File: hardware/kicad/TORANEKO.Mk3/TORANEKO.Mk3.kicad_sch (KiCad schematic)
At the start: 85 parts, among them IC1 MP6551GQB-P, IC2 MP6551GQB-P, IC3 NCR321PASX, IC4 NCR321PASX, IC5 AS5047P-ATSM, IC6 STM32F411CEU6TR, IC7 AS5047P-ATSM, IC8 NCR321PASX, IC9 NCR321PASX, J1 Conn_01x02_Pin, J2 Conn_01x02_Pin, J3 Conn_01x02_Male, J5 Conn_01x02_Pin, J6 Conn_02x03_Odd_Even, Q1 IRLML6402, Q5 IRLML6344, SW1 SW_Push, U1 LSM6DSRXTR, U2 LXDC55FAAA-203, U3 Encord, U4 Encord_B, U5 Encord, U6 Encord_B, Y1 CSTNE10M0G52Z000R0

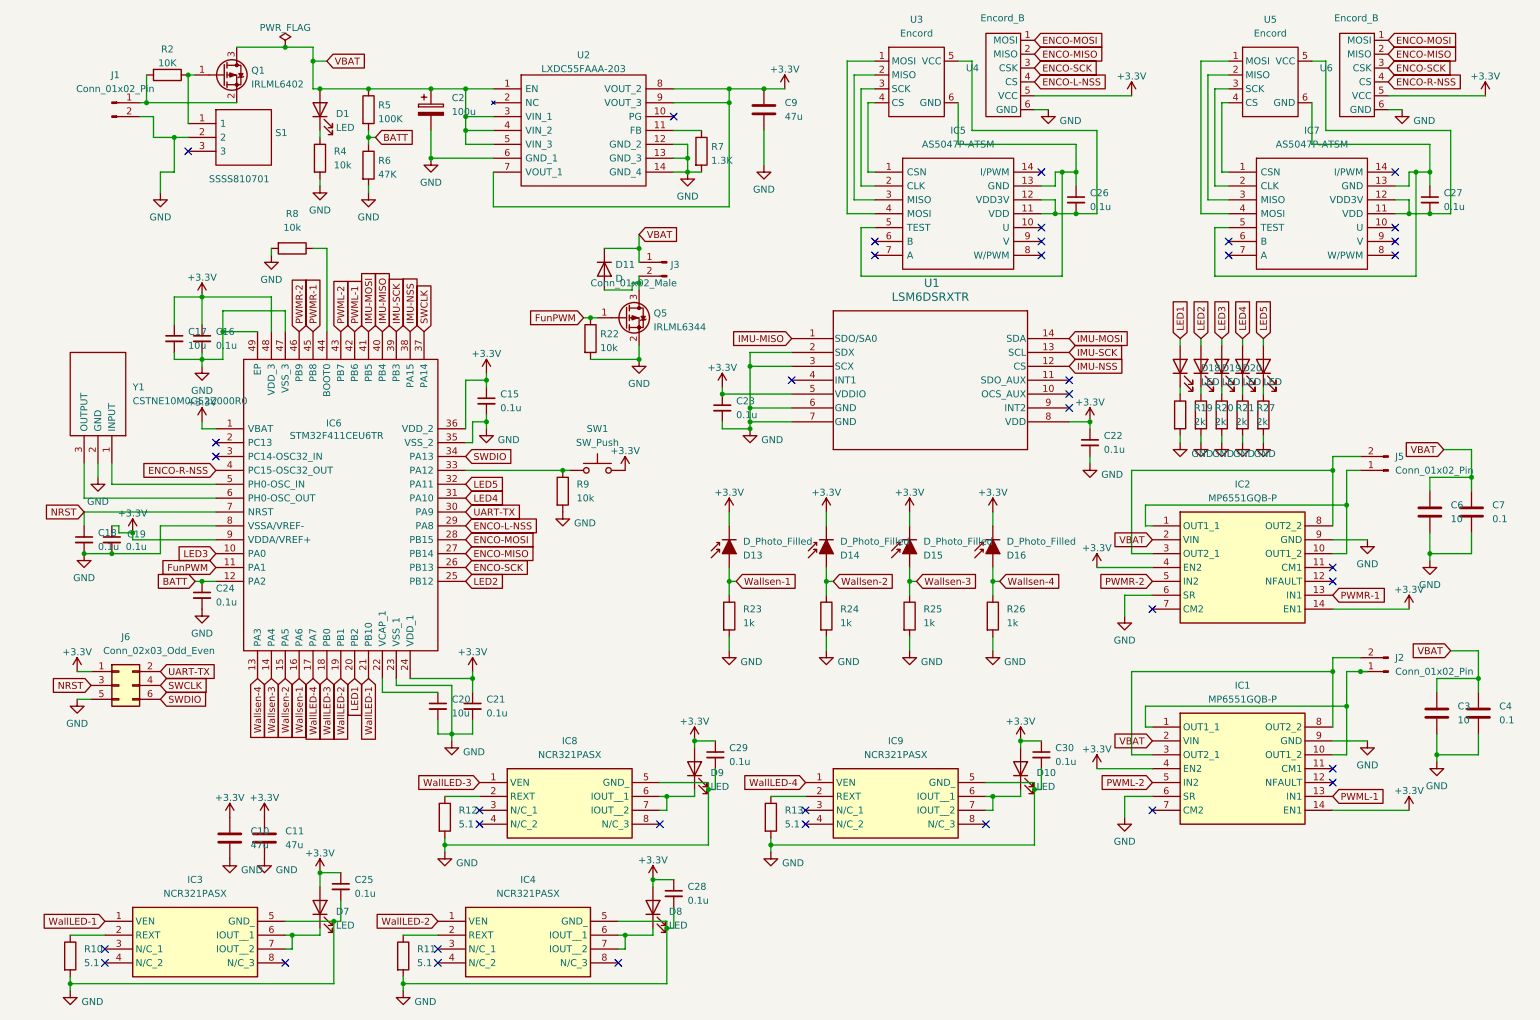
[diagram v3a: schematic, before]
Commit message: Start TORANEKO.Mk3 PCB layout; update schematic; add motor mount DXF
- Import schematic into PCB and start board layout (.kicad_pcb)
- Schematic: re-add LED/resistor pairs D23/R29, D24/R30 (2k) and connector J4;
  rework LED / WallLED global labels
- Add motor mount outline DXF

Co-Authored-By: Claude Opus 5.5 <noreply@anthropic.com>
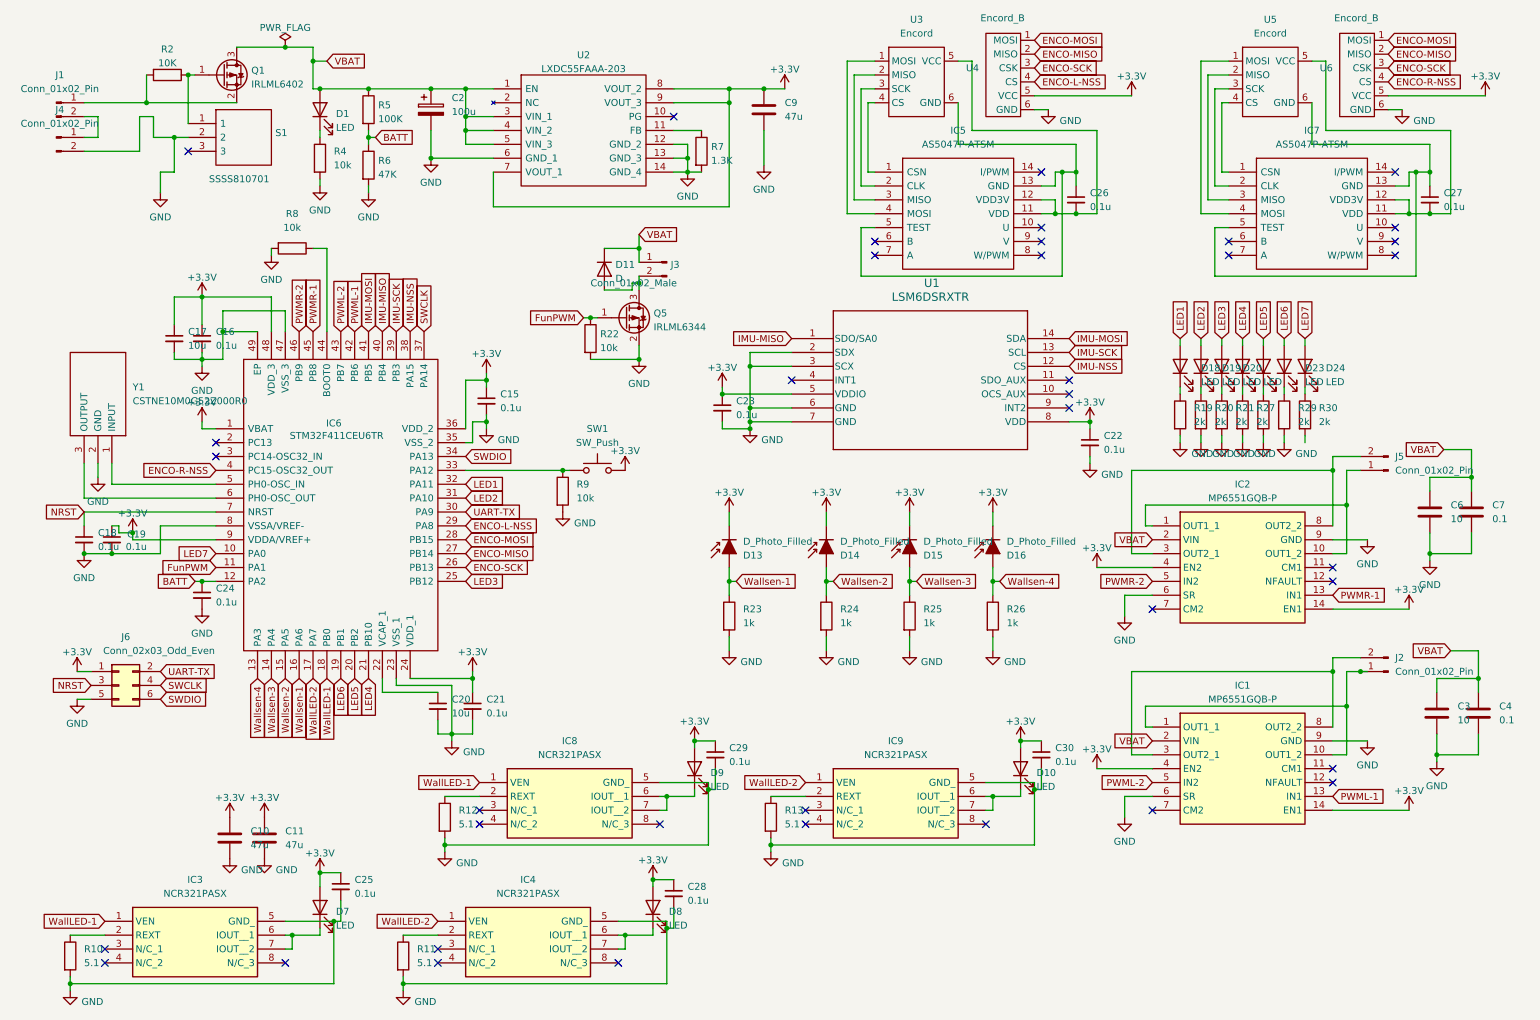
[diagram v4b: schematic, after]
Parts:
- added D23, D24: LED, LED_SMD:LED_0402_1005Metric, symbol Device:LED
- added J4: Conn_01x02_Pin, Connector_JST:JST_ZH_B2B-ZR_1x02_P1.50mm_Vertical, symbol Connector:Conn_01x02_Pin
- added R29, R30: 2k, Resistor_SMD:R_0402_1005Metric, symbol Device:R
- J1: footprint Connector_PinHeader_2.54mm:PinHeader_1x02_P2.54mm_Vertical -> Connector_JST:JST_ZH_B2B-ZR_1x02_P1.50mm_Vertical
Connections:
- net WallLED-3 is gone; now on net WallLED-1: IC6.18 (PB0), IC8.1 (VEN)
- net WallLED-4 is gone; now on net WallLED-2: IC6.17 (PA7), IC9.1 (VEN)
- net GND: now also J4.2 (Pin_2), R29.2; no longer J1.2 (Pin_2)
- net LED1: now also IC6.32 (PA11); no longer IC6.20 (PB2)
- net LED2: now also IC6.31 (PA10); no longer IC6.25 (PB12)
- net LED3: now also IC6.25 (PB12); no longer IC6.10 (PA0)
- net LED4: now also IC6.21 (PB10); no longer IC6.31 (PA10)
- net LED5: now also IC6.20 (PB2); no longer IC6.32 (PA11)
- net WallLED-1: no longer IC6.21 (PB10)
- net WallLED-2: no longer IC6.19 (PB1)
- new net: J1.2 (Pin_2), J4.1 (Pin_1)
- new net: D23.1 (K), R29.1
- new net: D24.1 (K), R30.1
- new net LED6: D23.2 (A), IC6.19 (PB1)
- new net LED7: D24.2 (A), IC6.10 (PA0)
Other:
- moved on the sheet: J1

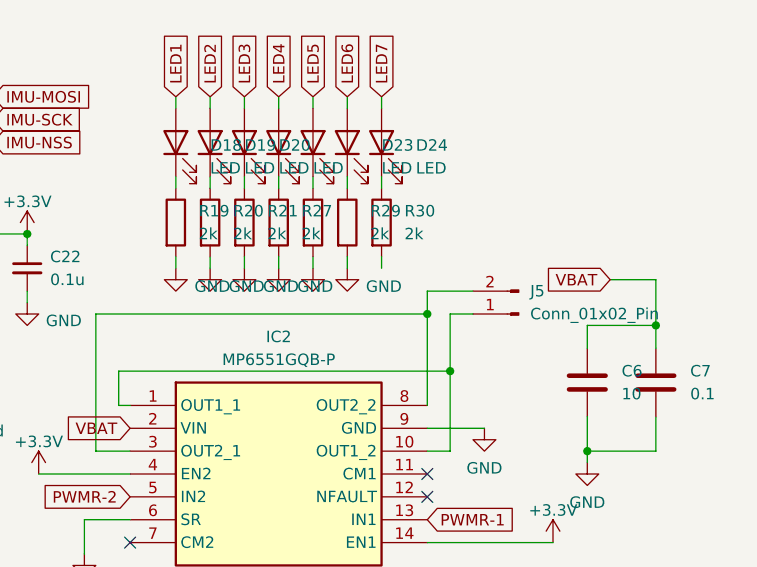
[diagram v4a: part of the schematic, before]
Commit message: Add GND symbol #PWR065 to TORANEKO.Mk3 schematic
- Add GND power symbol (#PWR065)
- Re-export schematic PDF

Co-Authored-By: Claude Opus 5.5 <noreply@anthropic.com>
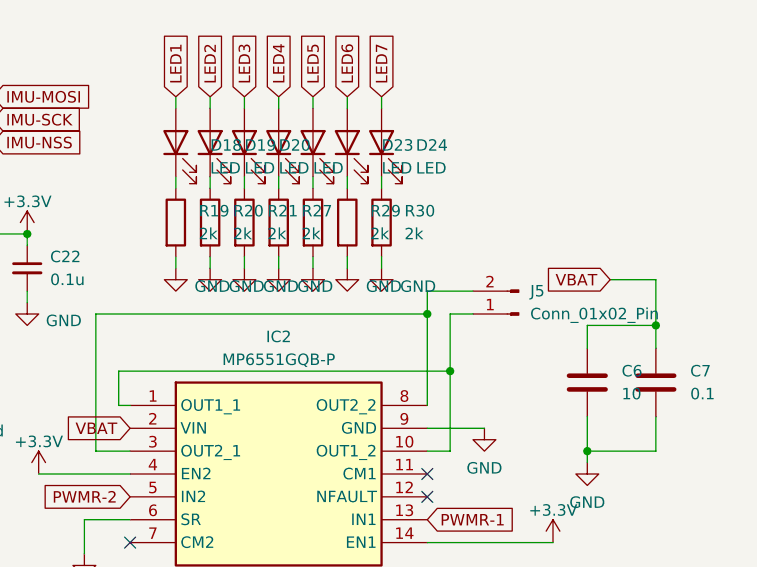
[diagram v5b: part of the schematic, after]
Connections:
- net GND: now also R30.2
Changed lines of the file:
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@@
+	)
+	(symbol
+		(lib_id "power:GND")
+		(at 245.11 92.71 0)
+		(unit 1)
+		(exclude_from_sim no)
+		(in_bom yes)
+		(on_board yes)
+		(dnp no)
+		(property "Reference" "#PWR065"
+			(at 245.11 99.06 0)
+			(effects
+				(font
+					(size 1.27 1.27)
+				)
+				(hide yes)
+			)
+		)
+		(property "Value" "GND"
+			(at 249.174 94.742 0)
+			(effects
+				(font
+					(size 1.27 1.27)
+				)
+			)
+		)
+		(property "Footprint" ""
+			(at 245.11 92.71 0)
+			(effects
+				(font
+					(size 1.27 1.27)
+				)
+				(hide yes)
+			)
+		)
+		(property "Datasheet" ""
+			(at 245.11 92.71 0)
+			(effects
+				(font
+					(size 1.27 1.27)
+				)
+				(hide yes)
+			)
+		)
+		(property "Description" ""
+			(at 245.11 92.71 0)
+			(effects
+				(font
+					(size 1.27 1.27)
+				)
+				(hide yes)
+			)
+		)
+		(pin "1"
+		)
+		(instances
+			(project "TORANEKO.Mk3"
+				(path "/326092ef-e572-4d1c-914e-fb52f7d8dea0"
+					(reference "#PWR065")
+					(unit 1)
+				)
+			)
+		)
 	)
 	(symbol

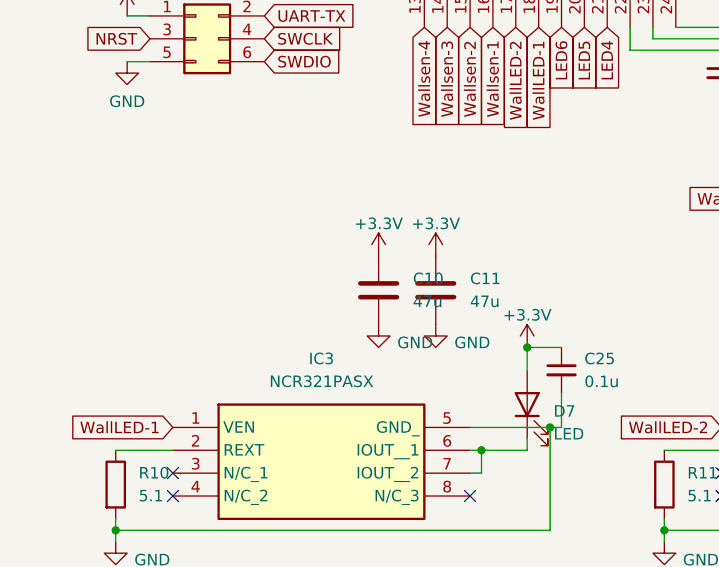
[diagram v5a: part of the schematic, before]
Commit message: Continue TORANEKO.Mk3 PCB layout and schematic update
- PCB layout progress (.kicad_pcb)
- Schematic updates (.kicad_sch)
- Change default via/pad size in project settings
- Ignore KiCad local history directory (.history/)

Co-Authored-By: Claude Opus 5.5 <noreply@anthropic.com>
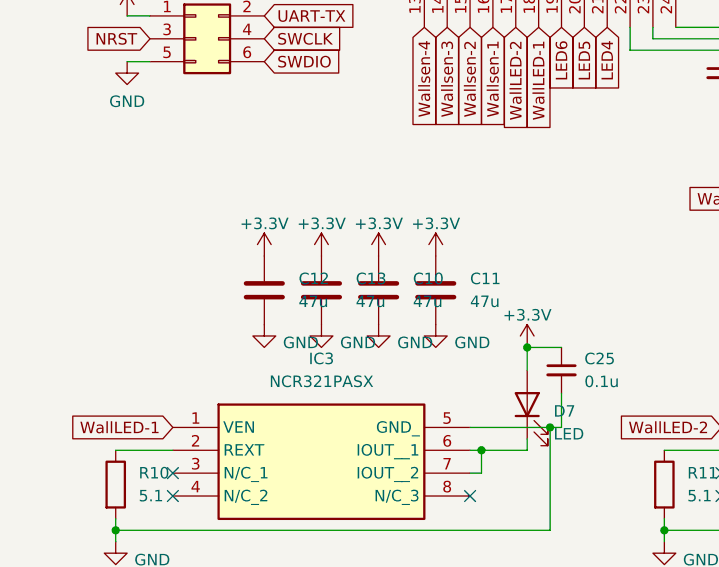
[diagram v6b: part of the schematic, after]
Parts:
- added C12, C13: 47u, Capacitor_SMD:C_0603_1608Metric, symbol Device:C
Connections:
- net +3.3V: now also C12.1, C13.1
- net GND: now also C12.2, C13.2

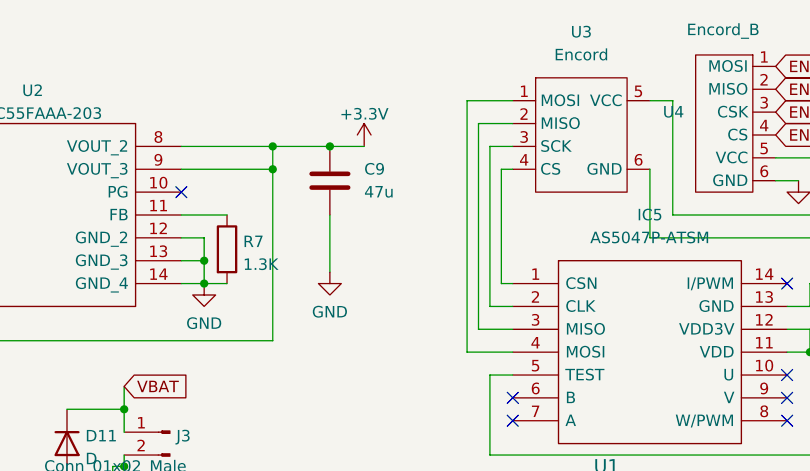
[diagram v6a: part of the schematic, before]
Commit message: Continue TORANEKO.Mk3 PCB layout; add C14 to schematic
- PCB layout progress (.kicad_pcb)
- Schematic: add 47u capacitor C14
- Add preset track widths (0.1/0.3/0.5/1.0/2.0 mm) to board setup
- Ignore KiCad autosave index (#auto_saved_files#)

Co-Authored-By: Claude Opus 5.5 <noreply@anthropic.com>
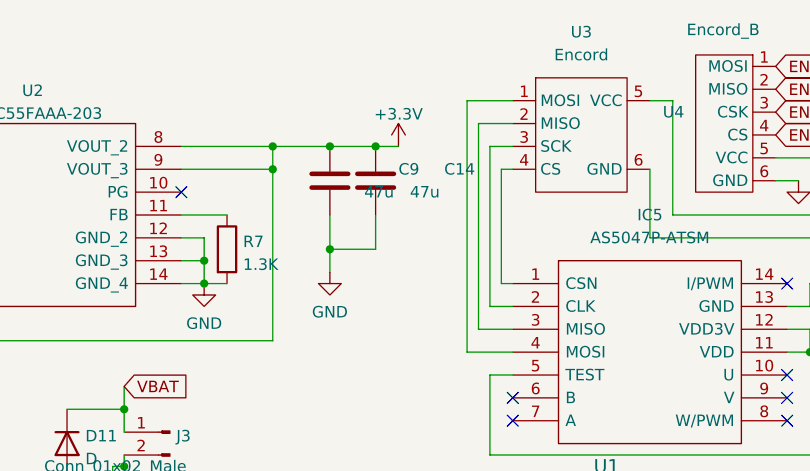
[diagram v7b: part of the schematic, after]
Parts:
- added C14: 47u, Capacitor_SMD:C_0603_1608Metric, symbol Device:C
- J3: footprint Connector_PinHeader_1.00mm:PinHeader_1x02_P1.00mm_Vertical -> Capacitor_SMD:C_0805_2012Metric
- U3: footprint Encorder-WG:Encord_L -> TORANEKO_Encoder:TN_ENC_Edge
- U4: footprint Encorder-WG:Encord_B_L -> TORANEKO_Encoder:TN_ENC_Base
- U5: footprint Encorder-WG:Encord -> TORANEKO_Encoder:TN_ENC_Edge
- U6: footprint Encorder-WG:Encord_B -> TORANEKO_Encoder:TN_ENC_Base
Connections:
- net +3.3V: now also C14.1
- net GND: now also C14.2
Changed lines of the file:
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@@
 	)
 	(junction
+		(at 146.05 39.37)
+		(diameter 0)
+		(color 0 0 0 0)
+	)
+	(junction
 		(at 95.25 81.28)
 		(diameter 0)
@@
 	)
 	(junction
+		(at 151.13 27.94)
+		(diameter 0)
+		(color 0 0 0 0)
+	)
+	(junction
 		(at 146.05 27.94)
 		(diameter 0)
@@
 	(wire
 		(pts
-			(xy 149.86 27.94) (xy 146.05 27.94)
+			(xy 153.67 27.94) (xy 151.13 27.94)
 		)
 		(stroke
@@
 	(wire
 		(pts
+			(xy 151.13 27.94) (xy 146.05 27.94)
+		)
+		(stroke
+			(width 0)
+			(type default)
+		)
+	)
+	(wire
+		(pts
 			(xy 187.96 118.11) (xy 187.96 120.65)
 		)
@@
 	(wire
 		(pts
+			(xy 151.13 35.56) (xy 151.13 39.37)
+		)
+		(stroke
+			(width 0)
+			(type default)
+		)
+	)
+	(wire
+		(pts
 			(xy 147.32 166.37) (xy 147.32 167.64)
 		)
@@
 	(wire
 		(pts
-			(xy 146.05 35.56) (xy 146.05 41.91)
+			(xy 146.05 35.56) (xy 146.05 39.37)
 		)
 		(stroke
@@
 	(wire
 		(pts
+			(xy 151.13 39.37) (xy 146.05 39.37)
+		)
+		(stroke
+			(width 0)
+			(type default)
+		)
+	)
+	(wire
+		(pts
 			(xy 92.71 135.89) (xy 92.71 138.43)
 		)
@@
 	(wire
 		(pts
+			(xy 146.05 39.37) (xy 146.05 41.91)
+		)
+		(stroke
+			(width 0)
+			(type default)
+		)
+	)
+	(wire
+		(pts
 			(xy 166.37 53.34) (xy 163.83 53.34)
 		)
@@
 			)
 		)
-		(property "Footprint" "Encorder-WG:Encord_B_L"
+		(property "Footprint" "TORANEKO_Encoder:TN_ENC_Base"
 			(at 191.77 13.97 0)
 			(effects
@@
 			)
 		)
-		(property "Footprint" "Connector_PinHeader_1.00mm:PinHeader_1x02_P1.00mm_Vertical"
+		(property "Footprint" "Capacitor_SMD:C_0805_2012Metric"
 			(at 128.27 59.69 0)
 			(effects
@@
 			)
 		)
-		(property "Footprint" "Encorder-WG:Encord_L"
+		(property "Footprint" "TORANEKO_Encoder:TN_ENC_Edge"
 			(at 170.18 15.24 0)
 			(effects
@@
 			)
 		)
-		(property "Footprint" "Encorder-WG:Encord"
+		(property "Footprint" "TORANEKO_Encoder:TN_ENC_Edge"
 			(at 234.95 15.24 0)
 			(effects
@@
 	(symbol
 		(lib_id "power:+3.3V")
-		(at 149.86 27.94 0)
+		(at 153.67 27.94 0)
 		(unit 1)
 		(exclude_from_sim no)
@@
 		(fields_autoplaced yes)
 		(property "Reference" "#PWR0125"
-			(at 149.86 31.75 0)
+			(at 153.67 31.75 0)
 			(effects
 				(font
@@
 		)
 		(property "Value" "+3.3V"
-			(at 149.86 24.3642 0)
+			(at 153.67 24.3642 0)
 			(effects
 				(font
@@
 		)
 		(property "Footprint" ""
-			(at 149.86 27.94 0)
+			(at 153.67 27.94 0)
 			(effects
 				(font
@@
 		)
 		(property "Datasheet" ""
-			(at 149.86 27.94 0)
+			(at 153.67 27.94 0)
 			(effects
 				(font
@@
 		)
 		(property "Description" ""
-			(at 149.86 27.94 0)
+			(at 153.67 27.94 0)
 			(effects
 				(font
@@
 			)
 		)
-		(property "Footprint" "Encorder-WG:Encord_B"
+		(property "Footprint" "TORANEKO_Encoder:TN_ENC_Base"
 			(at 256.54 13.97 0)
 			(effects
@@
 		(on_board yes)
 		(dnp no)
-		(fields_autoplaced yes)
 		(property "Reference" "C9"
-			(at 149.86 30.4799 0)
+			(at 153.67 30.4799 0)
 			(effects
 				(font
@@
 					(unit 1)
 				)
+			)
+		)
+	)
+	(symbol
+		(lib_id "Device:C")
+		(at 151.13 31.75 0)
+		(unit 1)
+		(exclude_from_sim no)
+		(in_bom yes)
+		(on_board yes)
+		(dnp no)
+		(property "Reference" "C14"
+			(at 158.75 30.4799 0)
+			(effects
+				(font
+					(size 1.27 1.27)
+				)
+				(justify left)
+			)
+		)
+		(property "Value" "47u"
+			(at 154.94 33.0199 0)
+			(effects
+				(font
+					(size 1.27 1.27)
+				)
+				(justify left)
+			)
+		)
+		(property "Footprint" "Capacitor_SMD:C_0603_1608Metric"
+			(at 152.0952 35.56 0)
+			(effects
+				(font
+					(size 1.27 1.27)
+				)
+				(hide yes)
+			)
+		)
+		(property "Datasheet" "~"
+			(at 151.13 31.75 0)
+			(effects
+				(font
+					(size 1.27 1.27)
+				)
+				(hide yes)
+			)
+		)
+		(property "Description" ""
+			(at 151.13 31.75 0)
+			(effects
+				(font
+					(size 1.27 1.27)
+				)
+				(hide yes)
+			)
+		)
+		(pin "1"
+		)
+		(pin "2"
+		)
+		(instances
+			(project "TORANEKO.Mk3"
+				(path "/326092ef-e572-4d1c-914e-fb52f7d8dea0"
+					(reference "C14")
+					(unit 1)
+				)

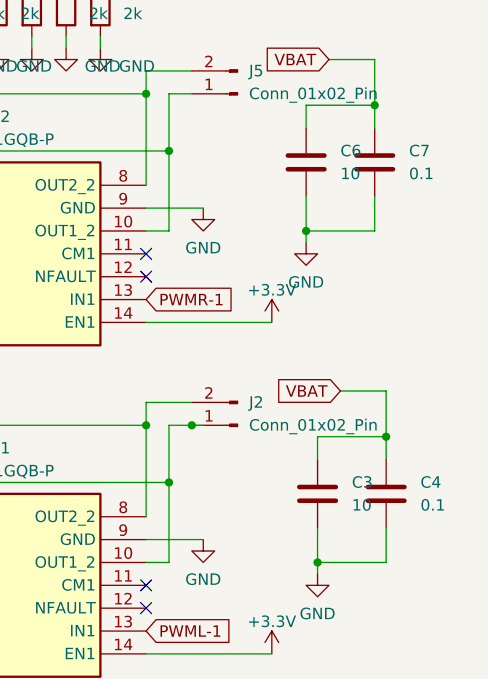
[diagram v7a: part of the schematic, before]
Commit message: Fix capacitor values in TORANEKO.Mk3 schematic/PCB (0.1 -> 0.1u, 10 -> 10u)
- Add missing "u" unit to two 0.1u and two 10u capacitor values
- Sync updated values to the PCB

Co-Authored-By: Claude Opus 5.5 <noreply@anthropic.com>
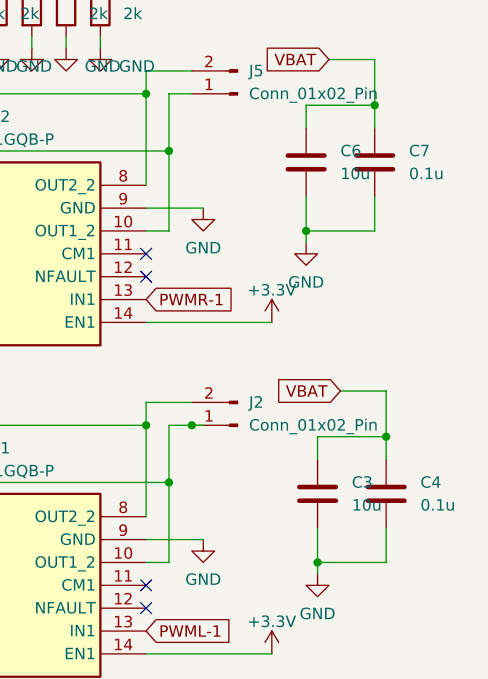
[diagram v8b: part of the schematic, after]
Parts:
- C3, C6: value 10 -> 10u
- C4, C7: value 0.1 -> 0.1u
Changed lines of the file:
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@@
 			)
 		)
-		(property "Value" "0.1"
+		(property "Value" "0.1u"
 			(at 280.67 143.5099 0)
 			(effects
@@
 			)
 		)
-		(property "Value" "10"
+		(property "Value" "10u"
 			(at 273.05 143.5099 0)
 			(effects
@@
 			)
 		)
-		(property "Value" "10"
+		(property "Value" "10u"
 			(at 271.78 106.6799 0)
 			(effects
@@
 			)
 		)
-		(property "Value" "0.1"
+		(property "Value" "0.1u"
 			(at 279.4 106.6799 0)
 			(effects
